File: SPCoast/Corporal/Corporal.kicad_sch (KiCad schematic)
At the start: 47 parts, among them SW783 783, SW795 795, SW799 799

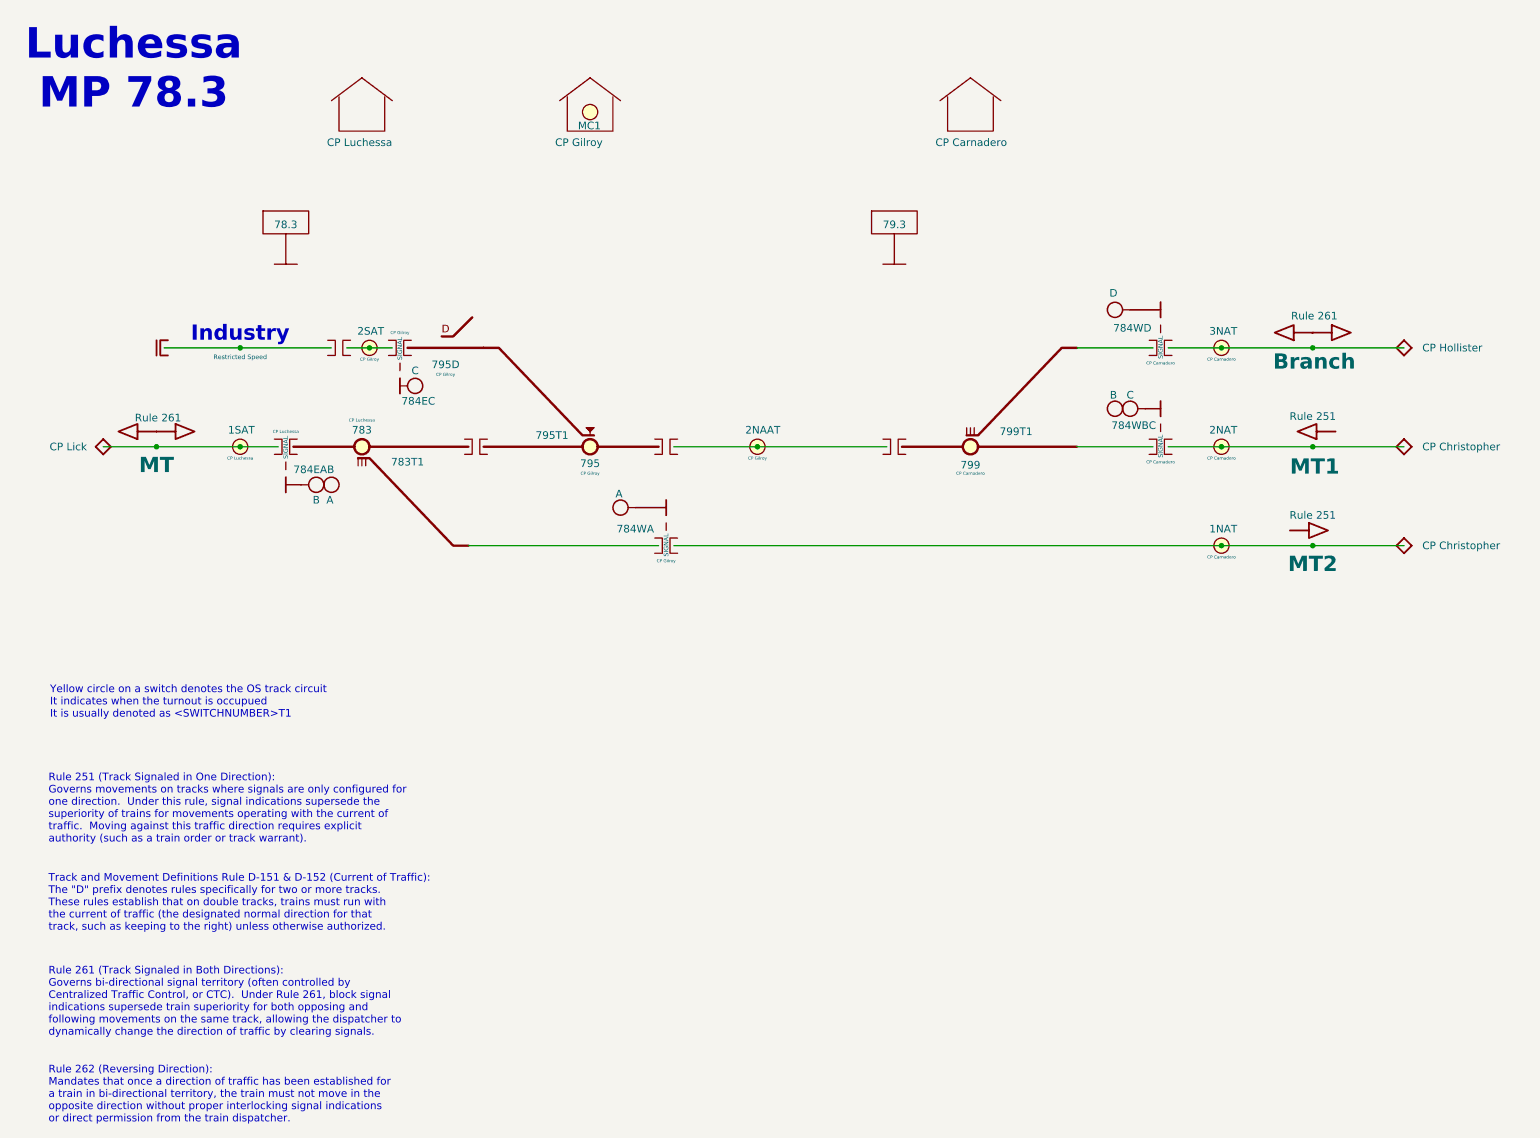
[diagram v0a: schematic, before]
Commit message: SPCoast: derail pin R, track circuit names end in T, code line symbols on the root sheet
Working-tree changes from the 2026-10-01..03 vocabulary review with
FieldUnit-Subdivision (docs/adr/0001-code-line-type-contract.md):

- Switch_Powered_Derail pin 2 is R (through path = REVERSE) in the seven
  plant schematics (library Railroad.kicad_sym renamed alongside; not in git)
- Luchessa track circuits renamed to end in T (1SAT, 2NAAT, ...); MC1 moved
  to CP Gilroy's house
- South-cTc: transports (MQTT, TimeCode, CMRInet, Loconet) on the root
  sheet on the CtcMachine Transports pin; field stations as encoding
  instances on the Luchessa sheet; two Luchessa lamp tokens renamed
- Six plant projects (Christopher, Corporal, GilroyCalTrain,
  GilroyInterchange, Sargent, Watsonville) added as drawn so far; Watsonville
  updated 2026-10-02

Co-Authored-By: Claude Fable 5.1 <noreply@anthropic.com>
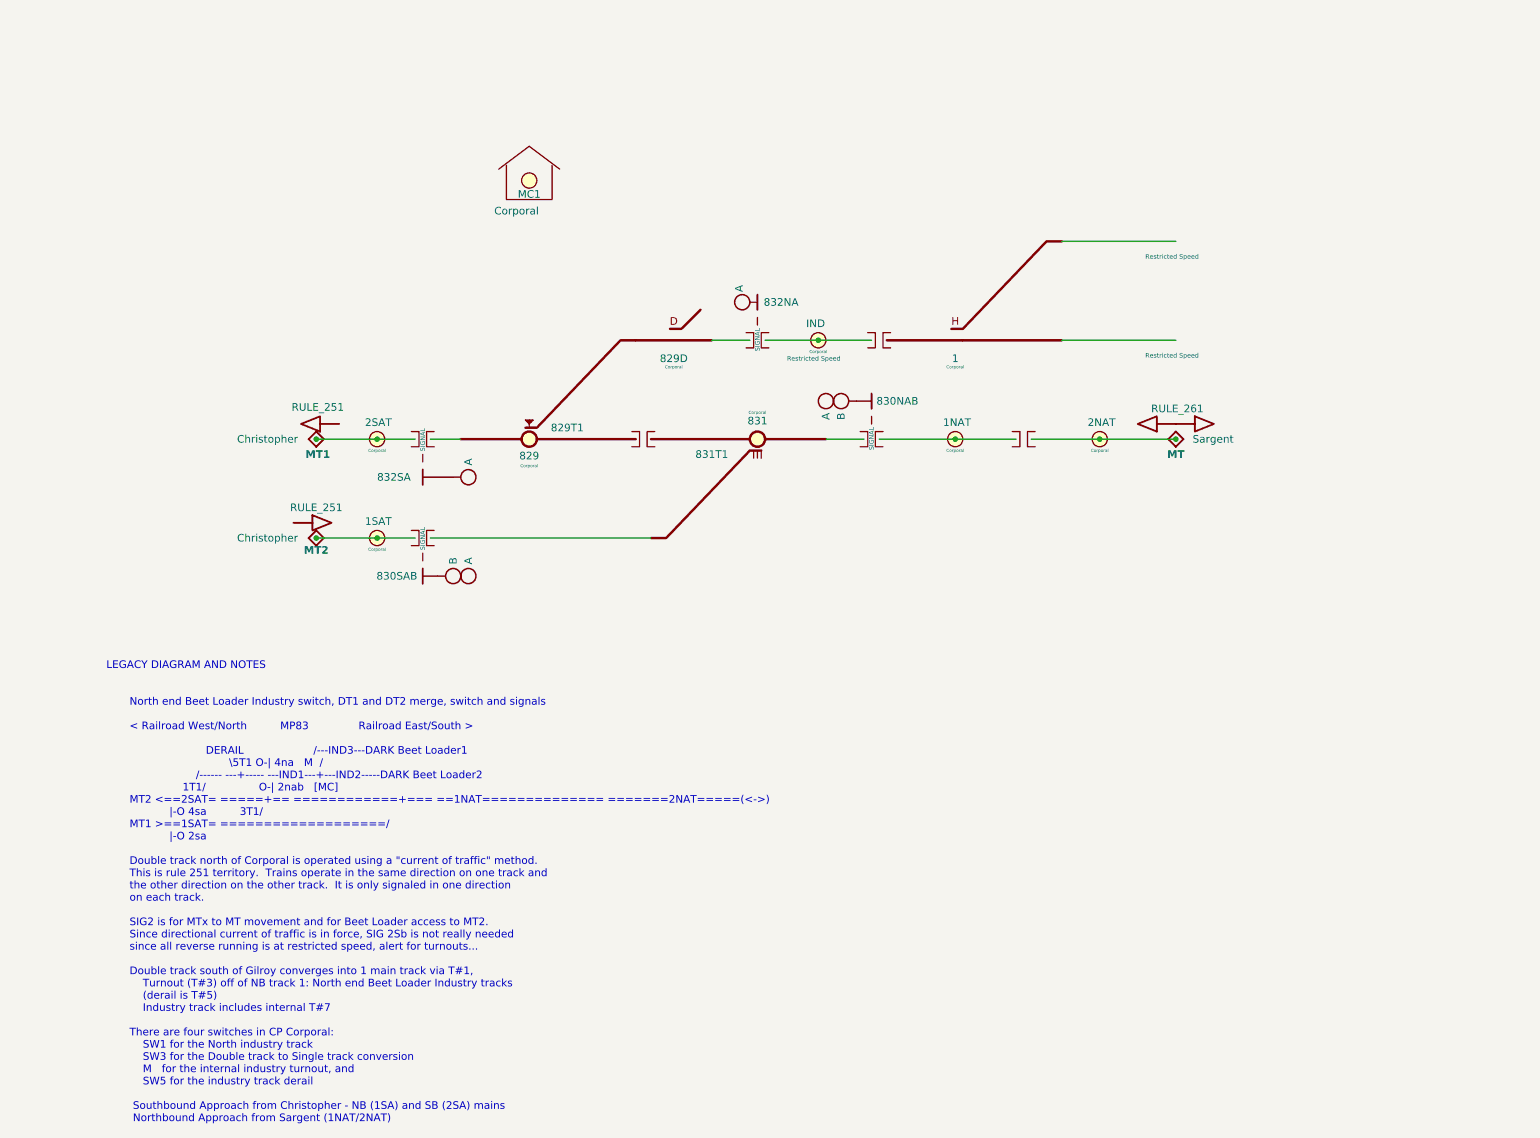
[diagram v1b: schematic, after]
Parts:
- removed B10, B2, B5: (no value), symbol Railroad:IRJ
- removed B3, B8, B9: (no value), symbol Railroad:IRJ-Signal
- removed B7: (no value), symbol Railroad:Bumper
- removed CP4: CP Christopher, symbol Railroad:NextCP
- removed DERAIL795: 795D, symbol Railroad:Switch_Powered_Derail
- removed DOT1: MT1, symbol Railroad:Rule251-DoT-Left
- removed DOT2: MT2, symbol Railroad:Rule251-DoT-Right
- removed DOT3: MT, symbol Railroad:Rule261-DoT-BiDirectional
- removed H7: B, symbol Railroad:Signal Head - CL
- removed H8: C, symbol Railroad:Signal Head - CL
- removed HOUSE2: CP Carnadero, symbol Railroad:MAIN HOUSE
- removed HOUSE3: CP Gilroy, symbol Railroad:MAIN HOUSE
- removed MP1: 79.3, symbol Railroad:Milepost
- removed MP2: 78.3, symbol Railroad:Milepost
- removed S784E1: 784EAB, symbol Railroad:Mast_Double
- removed S784E2: 784EC, symbol Railroad:Mast_Dwarf
- removed S784W1: 784WA, symbol Railroad:Mast_Single
- removed S784W2: 784WBC, symbol Railroad:Mast_Double
- removed S784W3: 784WD, symbol Railroad:Mast_Single
- removed SW783: 783, symbol Railroad:Switch_Powered
- removed SW795: 795, symbol Railroad:Switch_Lock
- removed SW799: 799, symbol Railroad:Switch_Powered
- removed TC6: 1SAT, symbol Railroad:Track Circuit
- added B2, B5: (no value), symbol Railroad:IRJ-Signal
- added B3, B7: (no value), symbol Railroad:IRJ
- added DOT1, DOT6: Restricted Speed, symbol Railroad:Rule105-RestrictedSpeed
- added DOT2: MT1, symbol Railroad:Rule251-DoT-Left
- added DOT3: MT2, symbol Railroad:Rule251-DoT-Right
- added H5: B, symbol Railroad:Signal Head - CL
- added S1: 832NA, symbol Railroad:Mast_Dwarf
- added S2: 830SAB, symbol Railroad:Mast_Double
- added S3: 832SA, symbol Railroad:Mast_Single
- added S4: 830NAB, symbol Railroad:Mast_Double
- added SW829: 829, symbol Railroad:Switch_Lock
- added SW831: 831, symbol Railroad:Switch_Powered
- added SW900: 829D, symbol Railroad:Switch_Powered_Derail
- added SW901: 1, symbol Railroad:Switch_HandThrow
- B1: CP CP Luchessa -> (none)
- B4: CP CP Gilroy -> (none)
- CP1: value CP Lick -> Sargent
- CP2: value CP Hollister -> Christopher
- CP3: value CP Christopher -> Christopher
- DOT4: value Branch -> MT; Rulebook 261 -> (none)
- H2: value B -> A
- H3: value C -> B
- H4: value D -> A
- HOUSE1: value CP Luchessa -> Corporal; Milepost 78.3 -> FIXME
- MC1: value (none) -> MC1
- TC1: value 3NAT -> 1NAT; CP CP Carnadero -> Corporal
- TC2: CP CP Carnadero -> Corporal
- TC3: value 1NAT -> 1SAT; CP CP Carnadero -> Corporal
- TC4: value 2NAAT -> 2SAT; CP CP Gilroy -> Corporal
- TC5: value 2SAT -> IND; CP CP Gilroy -> Corporal
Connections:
- net at DOT5.1 (To): now also SW901.2 (N)
- net at H4.1 (M): now also S2.3 (H1)
- net at CP3.1 (To): now also TC3.1 (MC), B2.2 (B), DOT3.1 (To); no longer TC2.1 (MC)
- net at B4.1 (A): now also SW900.2 (R)
- net at B4.2 (B), TC5.1 (MC): now also B3.1 (A), DOT6.1 (To)
- net at B4.3 (SIGNAL): now also S1.1 (SIGNAL)
- net at H6.1 (M): now also S4.3 (H1)
- net at H3.1 (M): now also S2.2 (H2)
- net at MC1.1 (MC): now also HOUSE1.1 (H)
- net at B6.2 (B): now also SW831.2 (N)
- net at H1.1 (M): now also S1.2 (H)
- net at B6.1 (A): now also SW829.2 (N); no longer TC4.1 (MC)
- net at B1.1 (A): now also SW829.1 (C)
- net at H2.1 (M): now also S3.2 (H)
- net at B1.2 (B): now also CP2.1 (To), TC4.1 (MC), DOT2.1 (To); no longer CP1.1 (To)
- net at B1.3 (SIGNAL): now also S3.1 (SIGNAL)
- new net: SW829.3 (R), SW900.1 (C)
- new net: H5.1 (M), S4.2 (H2)
- new net: B3.2 (B), SW901.1 (C)
- new net: B2.1 (A), SW831.3 (R)
- new net: B2.3 (SIGNAL), S2.1 (SIGNAL)
- new net: DOT1.1 (To), SW901.3 (R)
- new net: B5.3 (SIGNAL), S4.1 (SIGNAL)
- new net: B7.2 (B), CP1.1 (To), DOT4.1, TC2.1 (MC)
- new net: B5.1 (A), SW831.1 (C)
- new net: B5.2 (B), B7.1 (A), TC1.1 (MC)
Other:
- note added: "LEGACY DIAGRAM AND NOTES North end Beet Loader Industry switch, DT1 and DT2 merge, switch and signals < Railroad West/North MP83 Railroad East/South > DERAIL /---IND3---DARK Beet Loader1 \5T1 O-| 4na M / /------ ---+----- ---IND1---+---IND2-----DARK Beet Loader2 1T1/ O-| 2nab [MC] MT2 <==2SAT= =====+== ============+=== ==1NAT============== =======2NAT=====(<->) |-O 4sa 3T1/ MT1 >==1SAT= =========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"
- note removed: "Industry"
- note removed: "Luchessa MP 78.3"
- note removed: "Rule 251 (Track Signaled in One Direction): Governs movements on tracks where signals are only configured for one direction. Under this rule, signal indications supersede the superiority of trains for movements operating with the current of traffic. Moving against this traffic direction requires explicit authority (such as a train order or track warrant)."
- note removed: "Rule 261 (Track Signaled in Both Directions): Governs bi-directional signal territory (often controlled by Centralized Traffic Control, or CTC). Under Rule 261, block signal indications supersede train superiority for both opposing and following movements on the same track, allowing the dispatcher to dynamically change the direction of traffic by clearing signals."
- note removed: "Rule 262 (Reversing Direction): Mandates that once a direction of traffic has been established for a train in bi-directional territory, the train must not move in the opposite direction without proper interlocking signal indications or direct permission from the train dispatcher."
- note removed: "Track and Movement Definitions Rule D-151 & D-152 (Current of Traffic): The "D" prefix denotes rules specifically for two or more tracks. These rules establish that on double tracks, trains must run with the current of traffic (the designated normal direction for that track, such as keeping to the right) unless otherwise authorized."
- note removed: "Yellow circle on a switch denotes the OS track circuit It indicates when the turnout is occupued It is usually denoted as <SWITCHNUMBER>T1"
- title: Luchessa -> Corporal
